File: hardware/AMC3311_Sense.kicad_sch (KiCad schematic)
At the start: 37 parts, among them J10 SSA-2-100A, J11 SSA-2-100A, J9 LZSR 80-P, U4 TLV9002QDRQ1

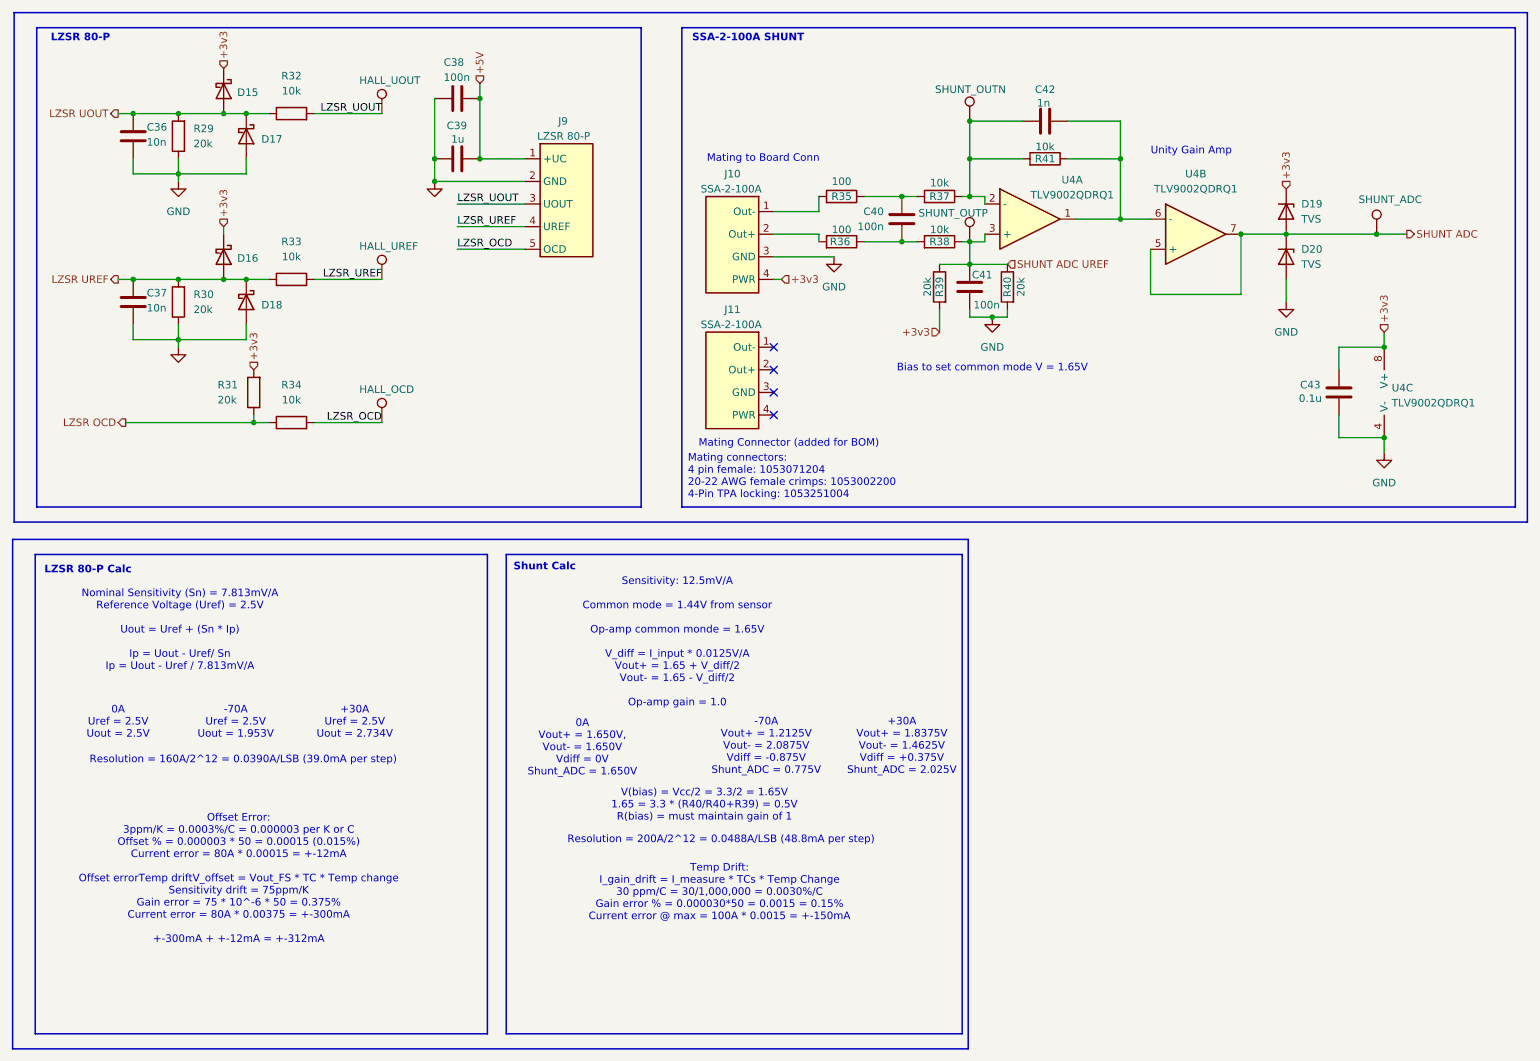
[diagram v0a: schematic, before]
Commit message: changed fully to 48 pin MCU
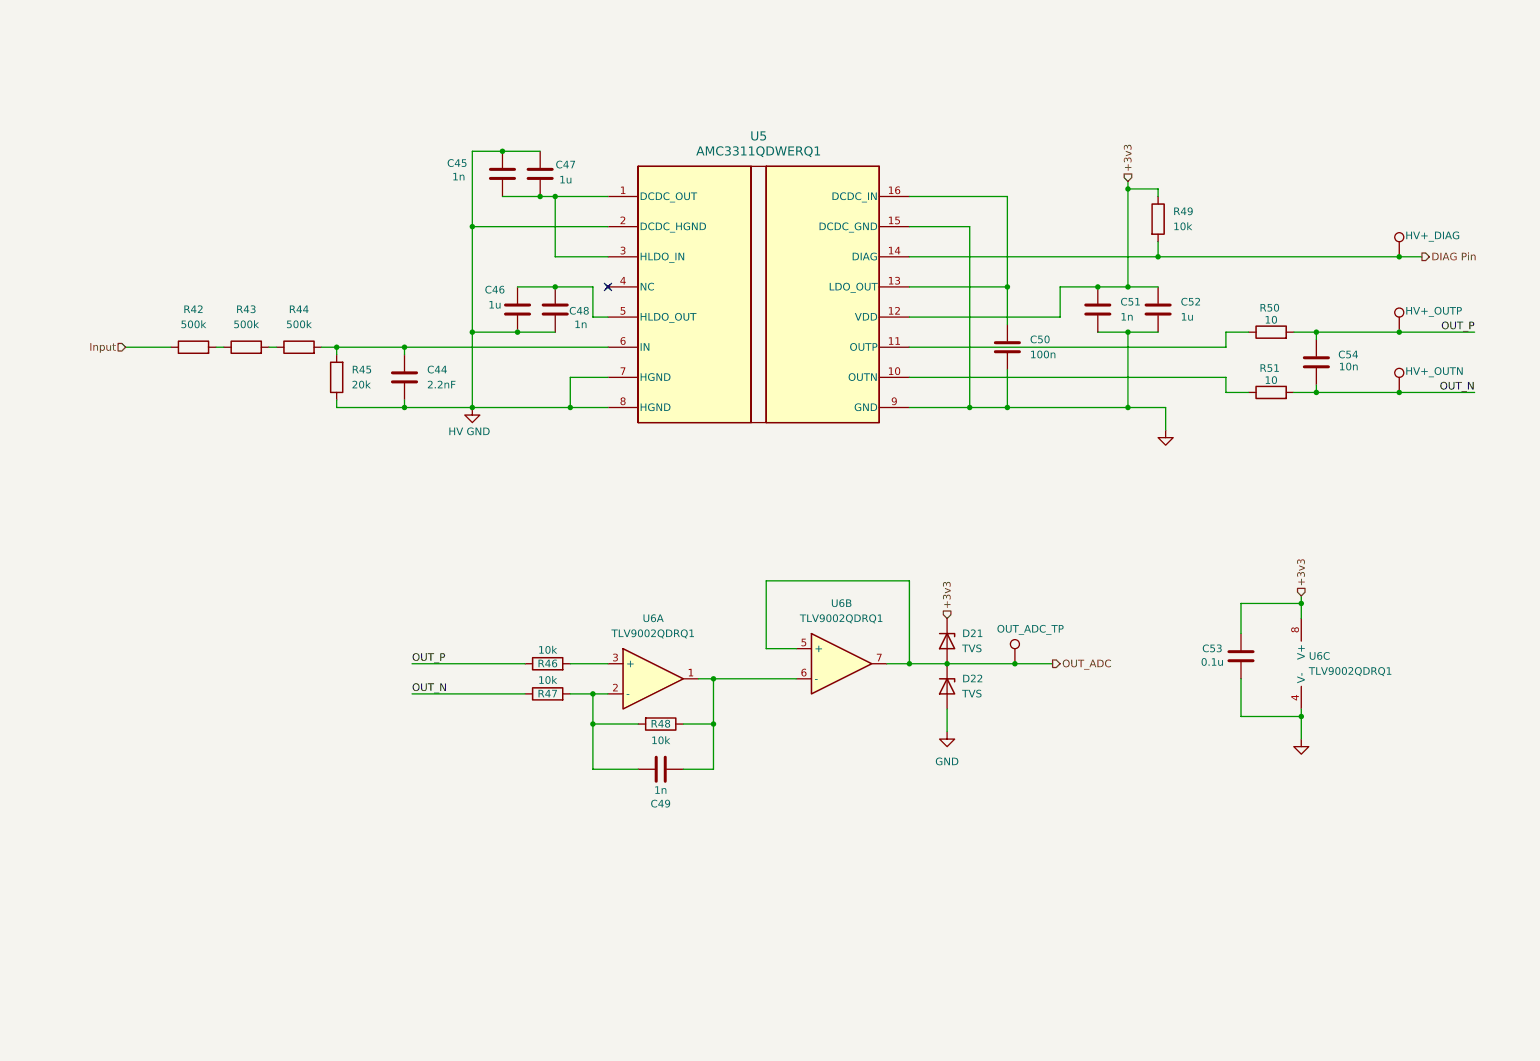
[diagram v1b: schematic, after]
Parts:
- removed C36, C37: 10n, symbol Device:C
- removed C38, C40, C41: 100n, symbol Device:C
- removed C39: 1u, symbol Device:C
- removed C42: 1n, symbol Device:C
- removed C43: 0.1u, symbol Device:C
- removed D15, D16, D17, D18: (no value), symbol Device:D_Schottky
- removed D19, D20: TVS, Diode_SMD:D_SOD-123F, symbol Device:D_Zener
- removed J10: SSA-2-100A, LHRS_Connectors:Molex_Nano-Fit_105309-xx04_1x04_P2.50mm_Vertical, symbol lhrs_connectors:CAN_NANO_01x05
- removed J11: SSA-2-100A, symbol lhrs_connectors:CAN_NANO_01x05
- removed J9: LZSR 80-P, LHRS_Connectors:Molex_Nano-Fit_105309-xx05_1x05_P2.50mm_Vertical, symbol lhrs_connectors:CAN_NANO_01x05
- removed R29, R30, R31, R39, R40: 20k, symbol Device:R
- removed R32, R33, R34, R37, R38, R41: 10k, symbol Device:R
- removed R35, R36: 100, symbol Device:R
- removed TP17: HALL_UOUT, symbol Connector:TestPoint
- removed TP18: HALL_UREF, symbol Connector:TestPoint
- removed TP19: HALL_OCD, symbol Connector:TestPoint
- removed TP20: SHUNT_OUTN, symbol Connector:TestPoint
- removed TP21: SHUNT_OUTP, symbol Connector:TestPoint
- removed TP22: SHUNT_ADC, symbol Connector:TestPoint
- removed U4: TLV9002QDRQ1, Package_SO:SOIC-8_3.9x4.9mm_P1.27mm, symbol lhrs_misc:TLV9002QDRQ1
- added C44: 2.2nF, symbol Device:C
- added C45, C48, C49, C51: 1n, symbol Device:C
- added C46, C47, C52: 1u, symbol Device:C
- added C50: 100n, symbol Device:C
- added C53: 0.1u, symbol Device:C
- added C54: 10n, symbol Device:C
- added D21, D22: TVS, Diode_SMD:D_SOD-123F, symbol Device:D_Zener
- added R42, R43, R44: 500k, symbol Device:R
- added R45: 20k, symbol Device:R
- added R46, R47, R48, R49: 10k, symbol Device:R
- added R50, R51: 10, symbol Device:R
- added TP23: OUT_ADC_TP, symbol Connector:TestPoint
- added TP24: HV+_DIAG, symbol Connector:TestPoint
- added TP25: HV+_OUTP, symbol Connector:TestPoint
- added TP26: HV+_OUTN, symbol Connector:TestPoint
- added U5: AMC3311QDWERQ1, AMC3311QDWERQ1:DWE0016A-IPC_A, symbol AMC3311QDWERQ1:AMC3311QDWERQ1
- added U6: TLV9002QDRQ1, Package_SO:SOIC-8_3.9x4.9mm_P1.27mm, symbol lhrs_misc:TLV9002QDRQ1
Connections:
- net +3v3: now also C51.1, C52.1, C53.1, D21.1 (K), R49.1, U5.12 (VDD), U6.8 (V+)
- net GND: now also C50.2, C51.2, C52.2, C53.2, D22.2 (A), U5.15 (DCDC_GND), U5.9 (GND), U6.4 (V-)
- new net: R51.1, U5.10 (OUTN)
- new net: R50.1, U5.11 (OUTP)
- new net: R42.2, R43.1
- new net: C49.1, R47.2, R48.2, U6.2 (-)
- new net: C49.2, R48.1, U6.1, U6.6 (-)
- new net: C46.2, C48.2, U5.5 (HLDO_OUT)
- new net: R43.2, R44.1
- new net: C44.1, R44.2, R45.2, U5.6 (IN)
- new net: C50.1, U5.13 (LDO_OUT), U5.16 (DCDC_IN)
- new net: R46.2, U6.3 (+)
- new net: C45.1, C47.2, U5.1 (DCDC_OUT), U5.3 (HLDO_IN)
- new net DIAG Pin: R49.2, TP24.1, U5.14 (DIAG)
- new net HV GND: C44.2, C45.2, C46.1, C47.1, C48.1, R45.1, U5.2 (DCDC_HGND), U5.7 (HGND), U5.8 (HGND)
- new net Input: R42.1
- new net OUT_ADC: D21.2 (A), D22.1 (K), TP23.1, U6.5 (+), U6.7
- new net OUT_N: C54.1, R47.1, R51.2, TP26.1
- new net OUT_P: C54.2, R46.1, R50.2, TP25.1
- no-connect marks 4 -> 1
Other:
- note removed: "+30A Uref = 2.5V Uout = 2.734V"
- note removed: "+30A Vout+ = 1.8375V Vout- = 1.4625V Vdiff = +0.375V Shunt_ADC = 2.025V"
- note removed: "-70A Uref = 2.5V Uout = 1.953V"
- note removed: "-70A Vout+ = 1.2125V Vout- = 2.0875V Vdiff = -0.875V Shunt_ADC = 0.775V"
- note removed: "0A Uref = 2.5V Uout = 2.5V"
- note removed: "0A Vout+ = 1.650V, Vout- = 1.650V Vdiff = 0V Shunt_ADC = 1.650V"
- note removed: "Bias to set common mode V = 1.65V"
- note removed: "LZSR 80-P"
- note removed: "LZSR 80-P Calc"
- note removed: "Mating Connector (added for BOM)"
- note removed: "Mating connectors: 4 pin female: 1053071204 20-22 AWG female crimps: 1053002200 4-Pin TPA locking: 1053251004"
- note removed: "Mating to Board Conn"
- note removed: "Nominal Sensitivity (Sn) = 7.813mV/A Reference Voltage (Uref) = 2.5V Uout = Uref + (Sn * Ip) Ip = Uout - Uref/ Sn Ip = Uout - Uref / 7.813mV/A"
- note removed: "Offset Error: 3ppm/K = 0.0003%/C = 0.000003 per K or C Offset % = 0.000003 * 50 = 0.00015 (0.015%) Current error = 80A * 0.00015 = +-12mA Offset errorTemp driftV_offset = Vout_FS * TC * Temp change Sensitivity drift = 75ppm/K Gain error = 75 * 10^-6 * 50 = 0.375% Current error = 80A * 0.00375 = +-300mA +-300mA + +-12mA = +-312mA"
- note removed: "Resolution = 160A/2^12 = 0.0390A/LSB (39.0mA per step)"
- note removed: "Resolution = 200A/2^12 = 0.0488A/LSB (48.8mA per step)"
- note removed: "SSA-2-100A SHUNT"
- note removed: "Sensitivity: 12.5mV/A Common mode = 1.44V from sensor Op-amp common monde = 1.65V V_diff = I_input * 0.0125V/A Vout+ = 1.65 + V_diff/2 Vout- = 1.65 - V_diff/2 Op-amp gain = 1.0"
- note removed: "Shunt Calc"
- note removed: "Temp Drift: I_gain_drift = I_measure * TCs * Temp Change 30 ppm/C = 30/1,000,000 = 0.0030%/C Gain error % = 0.000030*50 = 0.0015 = 0.15% Current error @ max = 100A * 0.0015 = +-150mA"
- note removed: "Unity Gain Amp"
- note removed: "V(bias) = Vcc/2 = 3.3/2 = 1.65V 1.65 = 3.3 * (R40/R40+R39) = 0.5V R(bias) = must maintain gain of 1"

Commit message: fixed ERC, made it look pretty
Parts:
- C44, C45, C46, C47, C48, C49, C50, C51, C52, C53, C54: footprint (none) -> Capacitor_SMD:C_0603_1608Metric_Pad1.08x0.95mm_HandSolder
- D19: renamed from D21; P/N SMF3.3 -> 576-SMF3.3
- D20: renamed from D22; P/N SMF3.3 -> 576-SMF3.3
- R42, R43, R44, R45: footprint (none) -> Resistor_SMD:R_0805_2012Metric_Pad1.20x1.40mm_HandSolder
- R46, R47, R48, R49, R50, R51: footprint (none) -> Resistor_SMD:R_0603_1608Metric_Pad0.98x0.95mm_HandSolder
- TP23, TP24, TP25, TP26: footprint (none) -> LHRS_Special:TestPoint_HEX_3mmID
- renumbered U5 to U8, U6 to U9

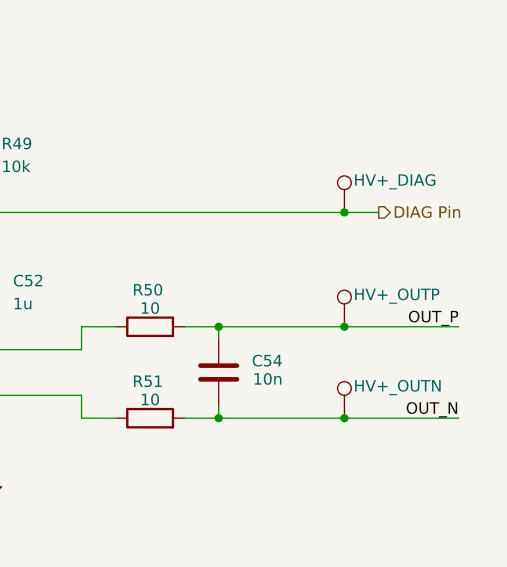
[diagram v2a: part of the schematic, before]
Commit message: added and updated all TP names
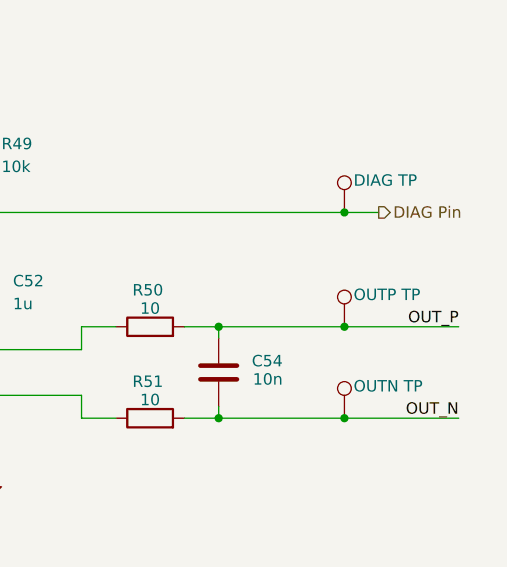
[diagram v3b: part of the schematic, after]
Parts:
- TP24: value HV+_DIAG -> DIAG TP
- TP25: value HV+_OUTP -> OUTP TP
- TP26: value HV+_OUTN -> OUTN TP
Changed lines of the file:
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@@
 			)
 		)
-		(property "Value" "HV+_OUTN"
+		(property "Value" "OUTN TP"
 			(at 249.936 76.454 0)
 			(show_name no)
@@
 			)
 		)
-		(property "Value" "HV+_DIAG"
+		(property "Value" "DIAG TP"
 			(at 249.936 53.594 0)
 			(show_name no)
@@
 			)
 		)
-		(property "Value" "HV+_OUTP"
+		(property "Value" "OUTP TP"
 			(at 249.936 66.294 0)
 			(show_name no)
